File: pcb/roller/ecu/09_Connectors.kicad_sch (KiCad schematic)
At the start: 11 parts, among them J6 TE-776163-1, J7 TE-776087-1, Q5 BSC065N06LS5, U2 LM74700

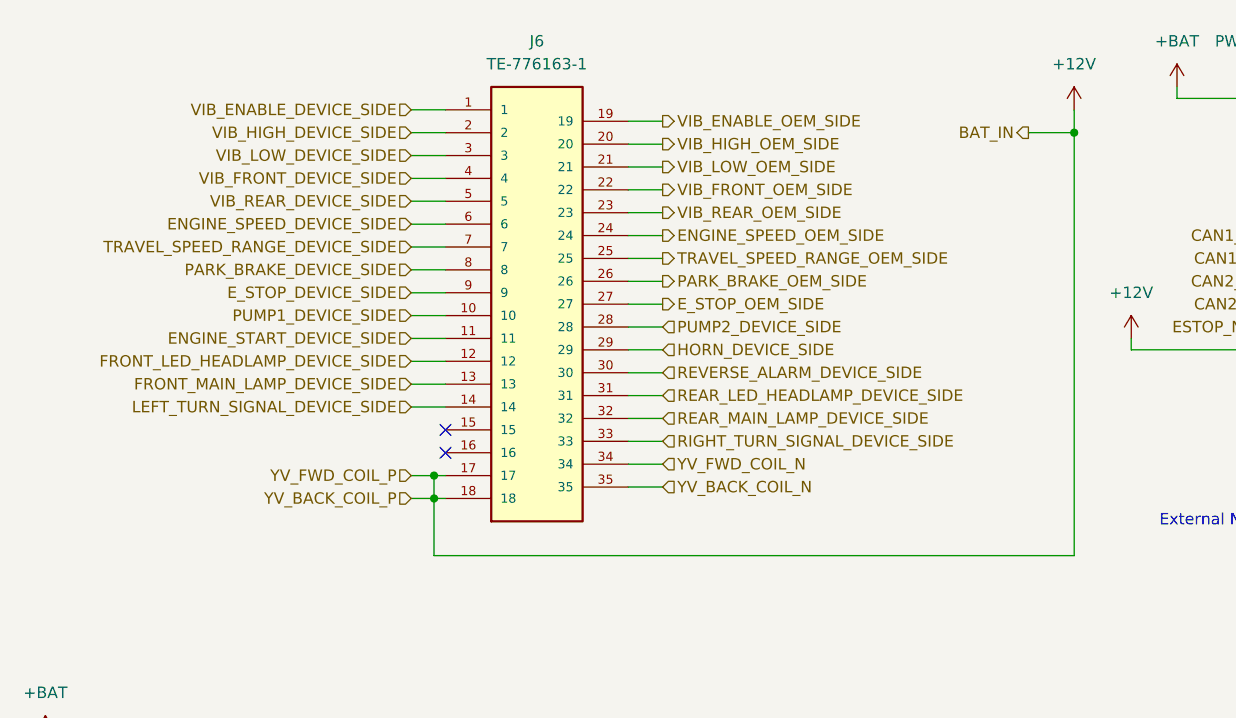
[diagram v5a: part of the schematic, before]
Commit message: feat: update ECU 4-layer layout and fabrication profile
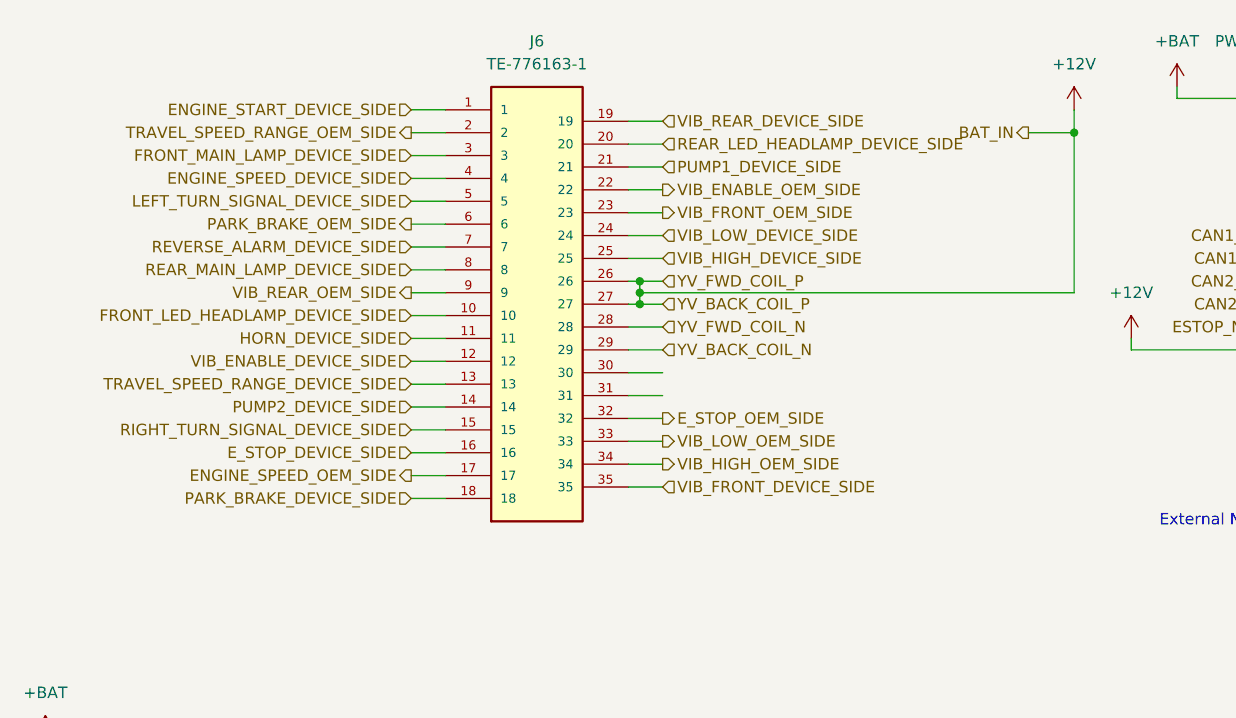
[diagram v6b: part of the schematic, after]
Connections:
- net +12V: now also J6.26, J6.27; no longer J6.17, J6.18
- net ENGINE_SPEED_DEVICE_SIDE: now also J6.4; no longer J6.6
- net ENGINE_SPEED_OEM_SIDE: now also J6.17; no longer J6.24
- net ENGINE_START_DEVICE_SIDE: now also J6.1; no longer J6.11
- net E_STOP_DEVICE_SIDE: now also J6.16; no longer J6.9
- net E_STOP_OEM_SIDE: now also J6.32; no longer J6.27
- net FRONT_LED_HEADLAMP_DEVICE_SIDE: now also J6.10; no longer J6.12
- net FRONT_MAIN_LAMP_DEVICE_SIDE: now also J6.3; no longer J6.13
- net HORN_DEVICE_SIDE: now also J6.11; no longer J6.29
- net LEFT_TURN_SIGNAL_DEVICE_SIDE: now also J6.5; no longer J6.14
- net PARK_BRAKE_DEVICE_SIDE: now also J6.18; no longer J6.8
- net PARK_BRAKE_OEM_SIDE: now also J6.6; no longer J6.26
- net PUMP1_DEVICE_SIDE: now also J6.21; no longer J6.10
- net PUMP2_DEVICE_SIDE: now also J6.14; no longer J6.28
- net REAR_LED_HEADLAMP_DEVICE_SIDE: now also J6.20; no longer J6.31
- net REAR_MAIN_LAMP_DEVICE_SIDE: now also J6.8; no longer J6.32
- net REVERSE_ALARM_DEVICE_SIDE: now also J6.7; no longer J6.30
- net RIGHT_TURN_SIGNAL_DEVICE_SIDE: now also J6.15; no longer J6.33
- net TRAVEL_SPEED_RANGE_DEVICE_SIDE: now also J6.13; no longer J6.7
- net TRAVEL_SPEED_RANGE_OEM_SIDE: now also J6.2; no longer J6.25
- net VIB_ENABLE_DEVICE_SIDE: now also J6.12; no longer J6.1
- net VIB_ENABLE_OEM_SIDE: now also J6.22; no longer J6.19
- net VIB_FRONT_DEVICE_SIDE: now also J6.35; no longer J6.4
- net VIB_FRONT_OEM_SIDE: now also J6.23; no longer J6.22
- net VIB_HIGH_DEVICE_SIDE: now also J6.25; no longer J6.2
- net VIB_HIGH_OEM_SIDE: now also J6.34; no longer J6.20
- net VIB_LOW_DEVICE_SIDE: now also J6.24; no longer J6.3
- net VIB_LOW_OEM_SIDE: now also J6.33; no longer J6.21
- net VIB_REAR_DEVICE_SIDE: now also J6.19; no longer J6.5
- net VIB_REAR_OEM_SIDE: now also J6.9; no longer J6.23
- net YV_BACK_COIL_N: now also J6.29; no longer J6.35
- net YV_FWD_COIL_N: now also J6.28; no longer J6.34
- no-connect marks 6 -> 4

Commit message: Add new resistor value and update used designators in ECU schematic
- Added a new resistor value of 0.8 to the list of available values.
- Updated the used designators to include J7 in the ECU schematic.
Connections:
- net +12V: now also J7.7; no longer J7.12
- net CAN1_H: now also J7.11; no longer J7.7
- net CAN1_L: now also J7.12; no longer J7.8
- net CAN2_H: now also J7.13; no longer J7.9
- net CAN2_L: now also J7.16; no longer J7.10
- net ENGINE_SENSOR_IN: now also J7.15; no longer J7.17
- net ESTOP_NC: now also J7.8; no longer J7.11
- net OIL_LEVEL_IN: now also J7.10; no longer J7.13
- net OIL_TEMP_IN: now also J7.9; no longer J7.14
- net SPEED_IN: now also J7.17; no longer J7.16
- net WATER_LEVEL_IN: now also J7.14; no longer J7.15
- removed net GND: H1.1, H2.1, H3.1, H4.1
- no-connect marks 4 -> 8

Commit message: Update used_designators in ecu.kicad_pro to include resistors R113-115
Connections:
- no-connect marks 8 -> 10
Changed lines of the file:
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@@
+	)
+	(no_connect
+		(at 106.68 82.55)
 	)
 	(no_connect
@@
 	)
 	(no_connect
+		(at 106.68 85.09)
+	)
+	(no_connect
